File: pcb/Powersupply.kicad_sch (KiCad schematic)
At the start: 37 parts, among them IC3 UCC28910DR, Q3 HL2303, U3 TPS54202DDC

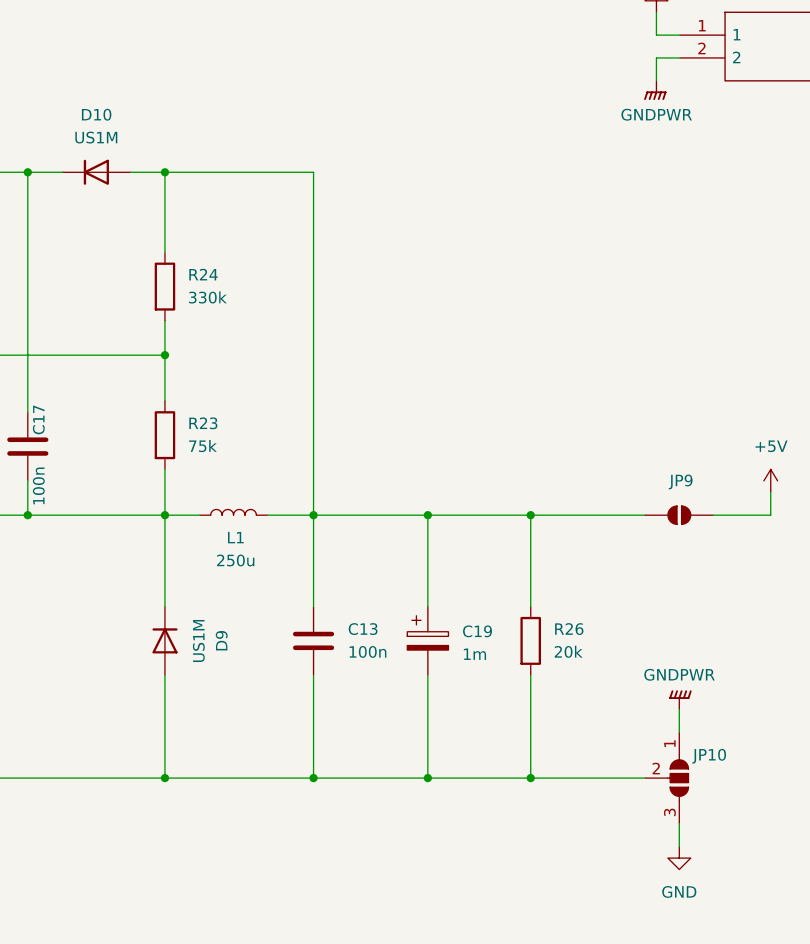
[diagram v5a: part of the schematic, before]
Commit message: added more stable output feedback to the ACDC converter
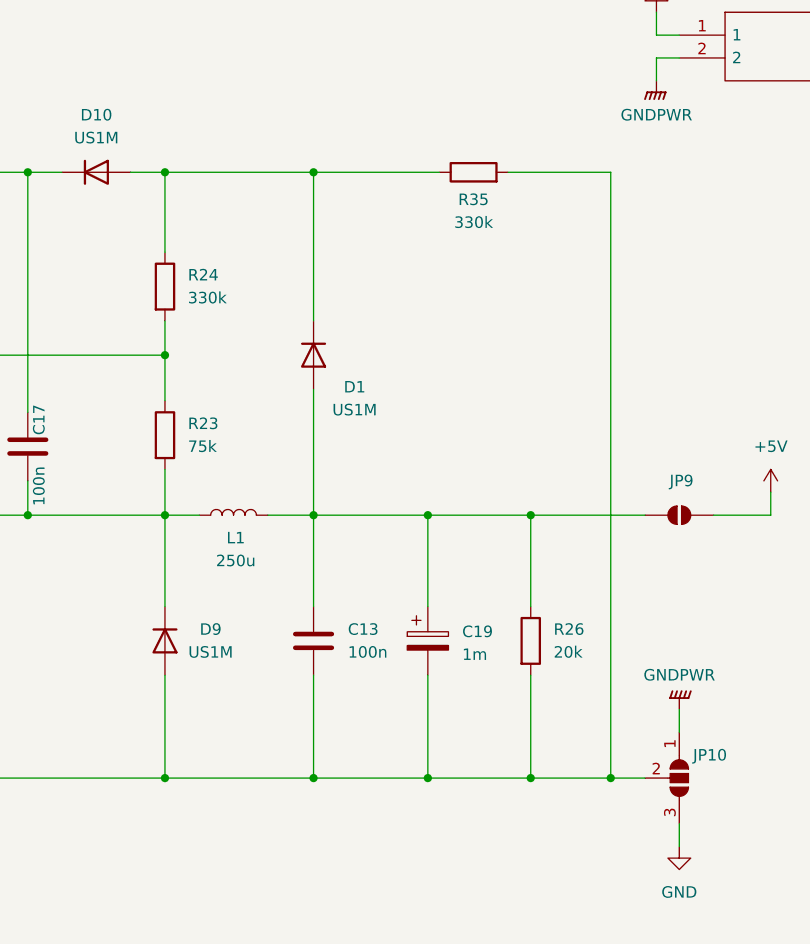
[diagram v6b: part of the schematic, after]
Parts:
- added D1: US1M, Diode_SMD:D_SMA, symbol Diode:US1M
- added R35: 330k, Resistor_SMD:R_0603_1608Metric, symbol Device:R
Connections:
- net RECT-: now also R35.2
- net at C13.1, C19.1, JP9.1 (A)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: now also D1.2 (A); no longer D10.2 (A), R24.1
- new net: D1.1 (K), D10.2 (A), R24.1, R35.1
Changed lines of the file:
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@@
 	)
 	(junction
+		(at 233.68 110.49)
+		(diameter 0)
+		(color 0 0 0 0)
+	)
+	(junction
 		(at 200.66 81.28)
 		(diameter 0)
@@
 		(color 0 0 0 0)
 	)
+	(junction
+		(at 200.66 43.18)
+		(diameter 0)
+		(color 0 0 0 0)
+	)
 	(no_connect
 		(at 115.57 78.74)
@@
 	(wire
 		(pts
-			(xy 200.66 43.18) (xy 184.15 43.18)
+			(xy 184.15 81.28) (xy 184.15 91.44)
 		)
 		(stroke
@@
 	(wire
 		(pts
-			(xy 184.15 81.28) (xy 184.15 91.44)
+			(xy 67.31 153.67) (xy 67.31 156.21)
 		)
 		(stroke
@@
 	(wire
 		(pts
-			(xy 67.31 153.67) (xy 67.31 156.21)
+			(xy 233.68 110.49) (xy 224.79 110.49)
+		)
+		(stroke
+			(width 0)
+			(type default)
+		)
+	)
+	(wire
+		(pts
+			(xy 233.68 43.18) (xy 233.68 110.49)
 		)
 		(stroke
@@
 	(wire
 		(pts
+			(xy 222.25 43.18) (xy 233.68 43.18)
+		)
+		(stroke
+			(width 0)
+			(type default)
+		)
+	)
+	(wire
+		(pts
+			(xy 200.66 43.18) (xy 200.66 59.69)
+		)
+		(stroke
+			(width 0)
+			(type default)
+		)
+	)
+	(wire
+		(pts
 			(xy 139.7 158.75) (xy 139.7 156.21)
 		)
@@
 	(wire
 		(pts
-			(xy 237.49 110.49) (xy 224.79 110.49)
+			(xy 237.49 110.49) (xy 233.68 110.49)
 		)
 		(stroke
@@
 	(wire
 		(pts
+			(xy 200.66 43.18) (xy 214.63 43.18)
+		)
+		(stroke
+			(width 0)
+			(type default)
+		)
+	)
+	(wire
+		(pts
 			(xy 167.64 177.8) (xy 167.64 176.53)
 		)
@@
 	(wire
 		(pts
-			(xy 200.66 81.28) (xy 200.66 43.18)
+			(xy 184.15 43.18) (xy 200.66 43.18)
 		)
 		(stroke
@@
 	(wire
 		(pts
+			(xy 200.66 67.31) (xy 200.66 81.28)
+		)
+		(stroke
+			(width 0)
+			(type default)
+		)
+	)
+	(wire
+		(pts
 			(xy 213.36 81.28) (xy 224.79 81.28)
 		)
@@
 		(dnp no)
 		(property "Reference" "D9"
-			(at 190.5 95.25 0)
+			(at 189.23 93.98 90)
 			(effects
 				(font
@@
 		)
 		(property "Value" "US1M"
-			(at 187.96 95.25 0)
+			(at 189.23 96.52 90)
 			(effects
 				(font
@@
 	)
 	(symbol
+		(lib_id "Device:R")
+		(at 218.44 43.18 90)
+		(unit 1)
+		(exclude_from_sim no)
+		(in_bom yes)
+		(on_board yes)
+		(dnp no)
+		(property "Reference" "R35"
+			(at 218.44 46.228 90)
+			(effects
+				(font
+					(size 1.27 1.27)
+				)
+			)
+		)
+		(property "Value" "330k"
+			(at 218.44 48.768 90)
+			(effects
+				(font
+					(size 1.27 1.27)
+				)
+			)
+		)
+		(property "Footprint" "Resistor_SMD:R_0603_1608Metric"
+			(at 218.44 44.958 90)
+			(effects
+				(font
+					(size 1.27 1.27)
+				)
+				(hide yes)
+			)
+		)
+		(property "Datasheet" "~"
+			(at 218.44 43.18 0)
+			(effects
+				(font
+					(size 1.27 1.27)
+				)
+				(hide yes)
+			)
+		)
+		(property "Description" "Resistor"
+			(at 218.44 43.18 0)
+			(effects
+				(font
+					(size 1.27 1.27)
+				)
+				(hide yes)
+			)
+		)
+		(pin "1"
+		)
+		(pin "2"
+		)
+		(instances
+			(project "ecu-dev-board"
+				(path "/38d4df77-b5a0-4642-8410-8b13c21c2c3b/59d7cd36-7b28-4e03-a153-4dfb2ab2e66a"
+					(reference "R35")
+					(unit 1)
+				)
+			)
+		)
+	)
+	(symbol
 		(lib_id "Jumper:SolderJumper_2_Open")
 		(at 35.56 29.21 0)
@@
 					(unit 1)
 				)
+			)
+		)
+	)
+	(symbol
+		(lib_id "Diode:US1M")
+		(at 200.66 63.5 270)
+		(unit 1)
+		(exclude_from_sim no)
+		(in_bom yes)
+		(on_board yes)
+		(dnp no)
+		(property "Reference" "D1"
+			(at 205.232 67.056 90)
+			(effects
+				(font
+					(size 1.27 1.27)
+				)
+			)
+		)
+		(property "Value" "US1M"
+			(at 205.232 69.596 90)
+			(effects
+				(font
+					(size 1.27 1.27)
+				)
+			)
+		)
+		(property "Footprint" "Diode_SMD:D_SMA"
+			(at 196.215 63.5 0)
+			(effects
+				(font
+					(size 1.27 1.27)
+				)
+				(hide yes)
+			)
+		)
+		(property "Datasheet" "https://www.diodes.com/assets/Datasheets/ds16008.pdf"
+			(at 200.66 63.5 0)
+			(effects
+				(font
+					(size 1.27 1.27)
+				)
+				(hide yes)
+			)
+		)
+		(property "Description" "1000V, 1A, General Purpose Rectifier Diode, SMA(DO-214AC)"
+			(at 200.66 63.5 0)
+			(effects
+				(font
+					(size 1.27 1.27)
+				)
+				(hide yes)
+			)
+		)
+		(property "Sim.Device" "D"
+			(at 200.66 63.5 0)
+			(effects
+				(font
+					(size 1.27 1.27)
+				)
+				(hide yes)
+			)
+		)
+		(property "Sim.Pins" "1=K 2=A"
+			(at 200.66 63.5 0)
+			(effects
+				(font
+					(size 1.27 1.27)
+				)
+				(hide yes)
+			)
+		)
+		(pin "2"
+		)
+		(pin "1"
+		)
+		(instances
+			(project "ecu-dev-board"
+				(path "/38d4df77-b5a0-4642-8410-8b13c21c2c3b/59d7cd36-7b28-4e03-a153-4dfb2ab2e66a"
+					(reference "D1")
+					(unit 1)
+				)

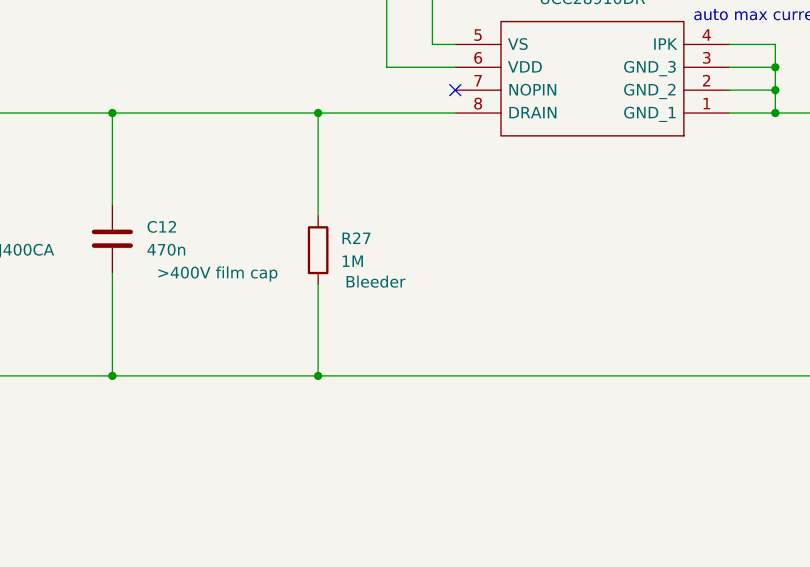
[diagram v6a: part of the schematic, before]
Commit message: change some resistor footprints to 0.25W compatible
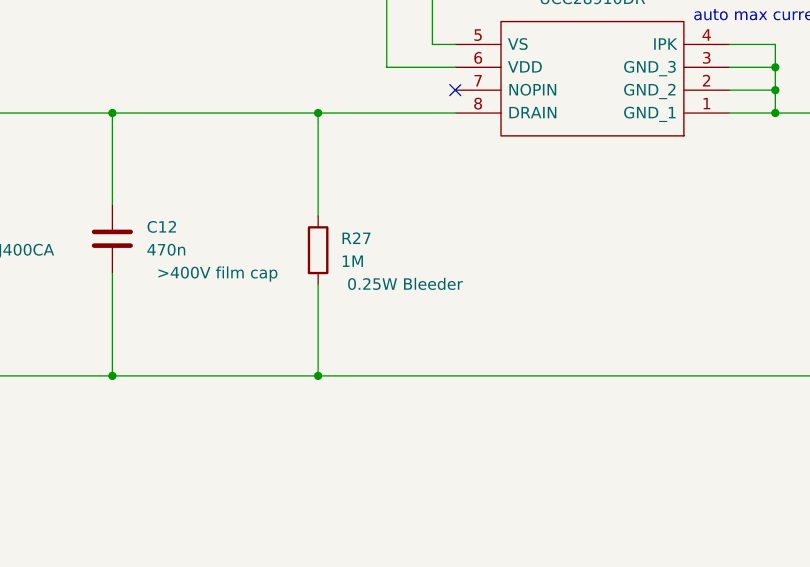
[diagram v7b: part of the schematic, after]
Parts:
- R27: footprint Resistor_SMD:R_0603_1608Metric -> Resistor_SMD:R_0805_2012Metric
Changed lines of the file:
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@@
 			)
 		)
-		(property "Footprint" "Resistor_SMD:R_0603_1608Metric"
+		(property "Footprint" "Resistor_SMD:R_0805_2012Metric"
 			(at 98.552 96.52 90)
 			(effects
@@
 			)
 		)
-		(property "Description" "Bleeder"
-			(at 106.68 100.076 0)
+		(property "Description" "0.25W Bleeder"
+			(at 109.982 100.33 0)
 			(effects
 				(font

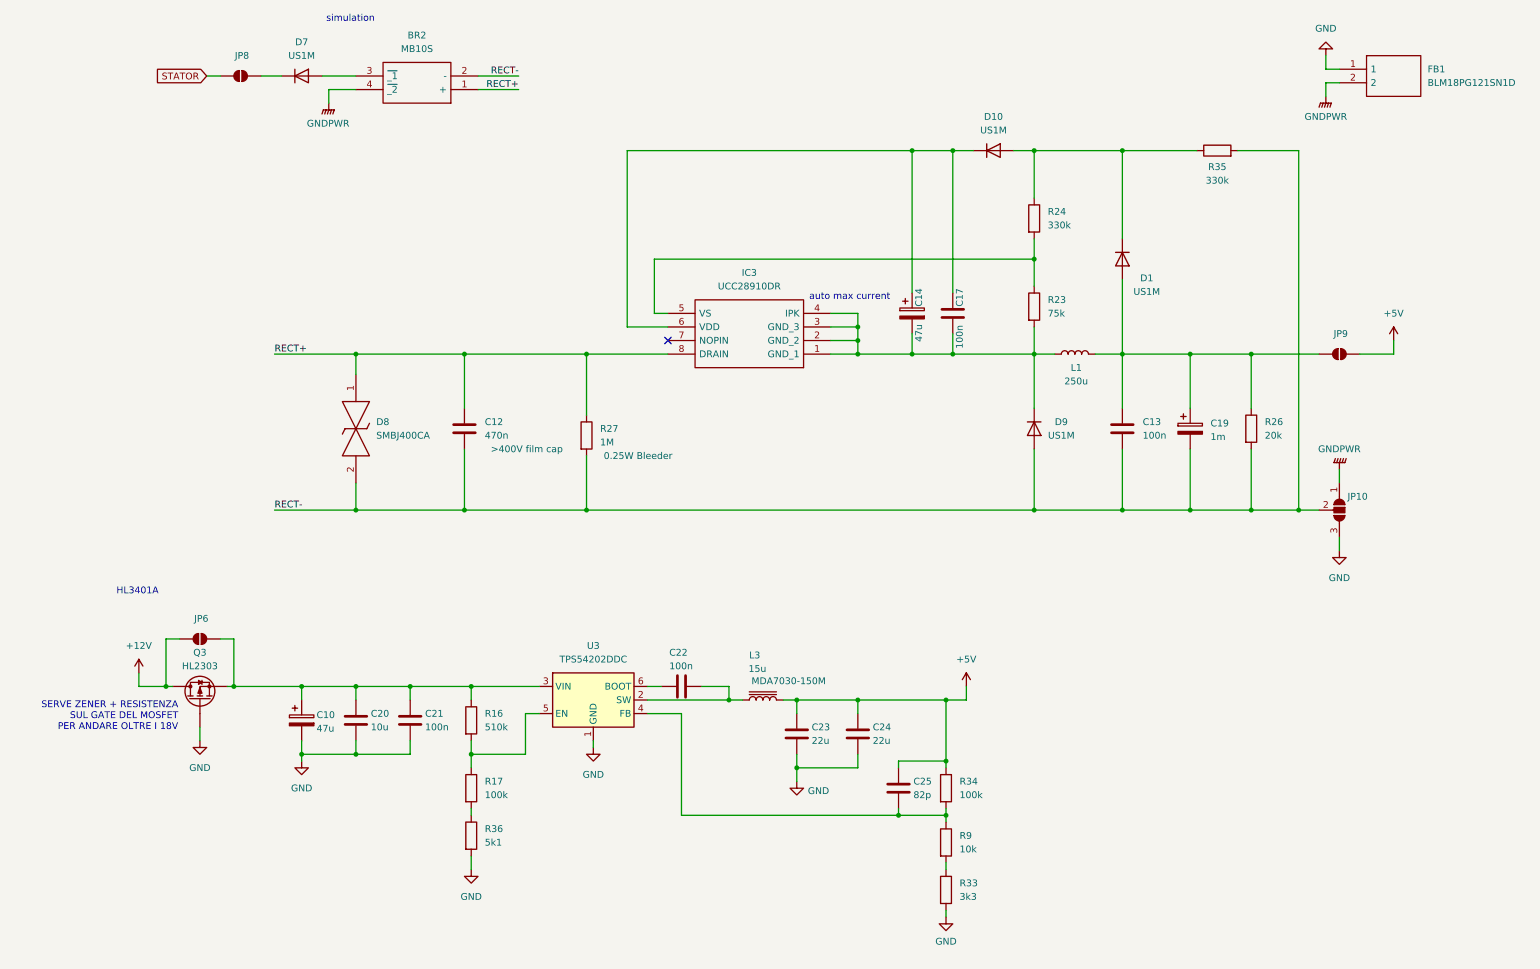
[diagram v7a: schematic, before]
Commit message: added PSU status LEDs and stator winding support
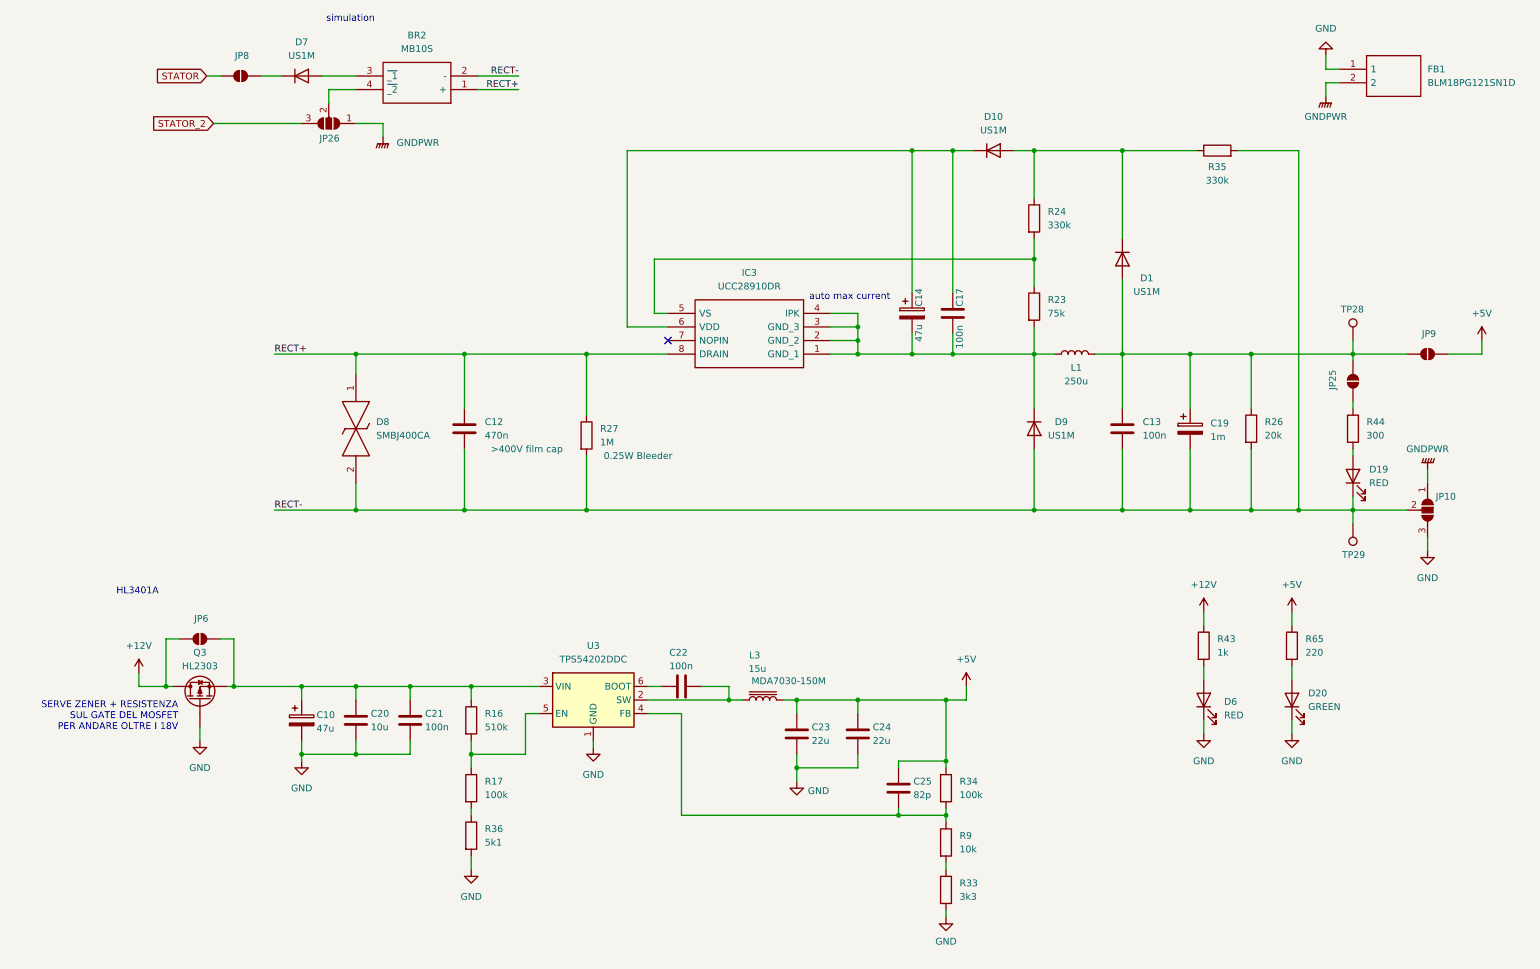
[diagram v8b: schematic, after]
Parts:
- added D19, D6: RED, symbol Device:LED
- added D20: GREEN, symbol Device:LED
- added JP25: SolderJumper_2_Open, Jumper:SolderJumper-2_P1.3mm_Open_RoundedPad1.0x1.5mm, symbol Jumper:SolderJumper_2_Open
- added JP26: SolderJumper_3_Open, Jumper:SolderJumper-3_P1.3mm_Open_RoundedPad1.0x1.5mm, symbol Jumper:SolderJumper_3_Open
- added R43: 1k, Resistor_SMD:R_0603_1608Metric, symbol Device:R
- added R44: 300, Resistor_SMD:R_0603_1608Metric, symbol Device:R
- added R65: 220, Resistor_SMD:R_0603_1608Metric, symbol Device:R
- added TP28, TP29: TestPoint, Connector_PinHeader_1.00mm:PinHeader_1x01_P1.00mm_Vertical, symbol Connector:TestPoint
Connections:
- net +12V: now also R43.1
- net +5V: now also R65.1
- net GND: now also D20.1 (K), D6.1 (K)
- net GNDPWR: now also JP26.1 (A); no longer BR2.4 (~{_2})
- net RECT-: now also D19.1 (K), TP29.1
- net at C13.1, C19.1, D1.2 (A)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: now also JP25.2 (B), TP28.1
- new net: D6.2 (A), R43.2
- new net: BR2.4 (~{_2}), JP26.2 (C)
- new net: D20.2 (A), R65.2
- new net: JP25.1 (A), R44.1
- new net: D19.2 (A), R44.2
- new net STATOR_2: JP26.3 (B)
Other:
- moved on the sheet: JP10, JP9
